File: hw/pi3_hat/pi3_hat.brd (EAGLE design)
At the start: 56.5 x 28.5 mm, 17 parts, among them U1 SINGLE-BIT_BUS_TRANSCEIVER, U2 SINGLE-BIT_BUS_TRANSCEIVER, U3 ST1S10, U4 DMMT5401, U5 DMG2305UX

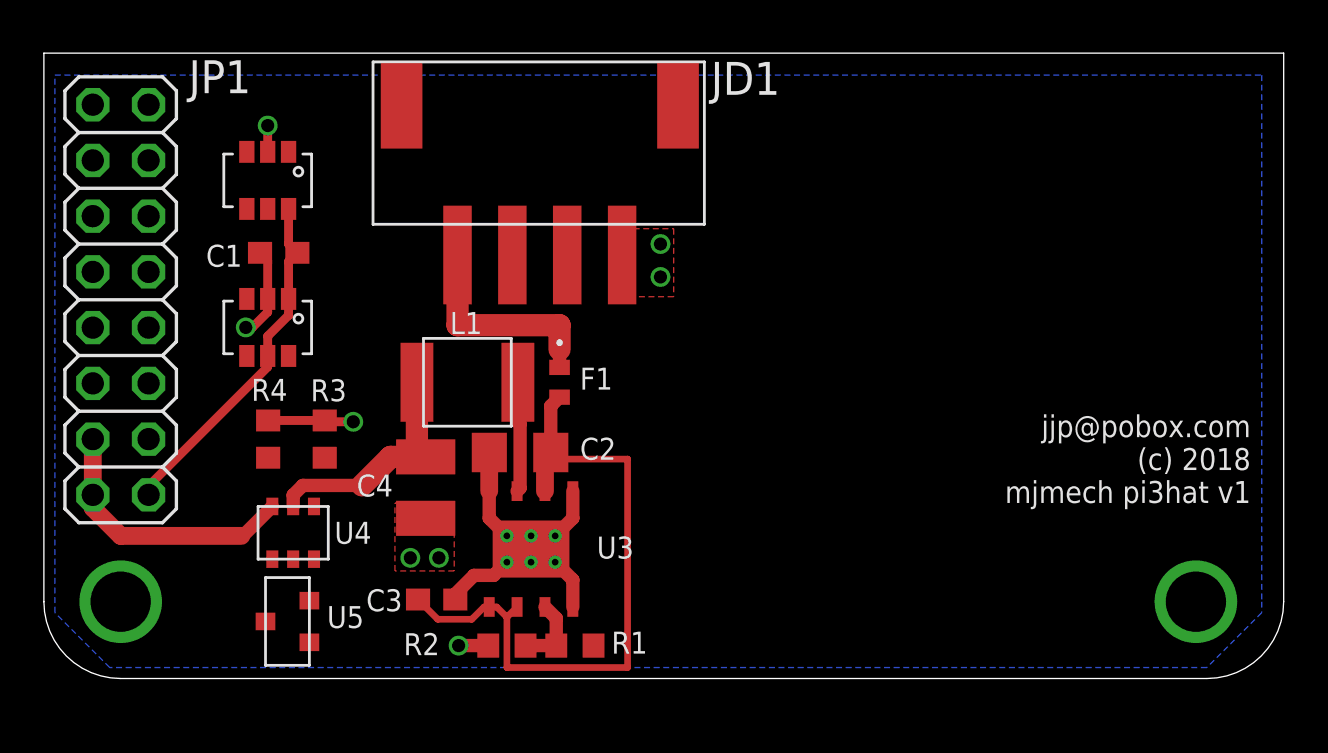
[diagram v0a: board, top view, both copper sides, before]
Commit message: rpi3 hat as sent to macrofab
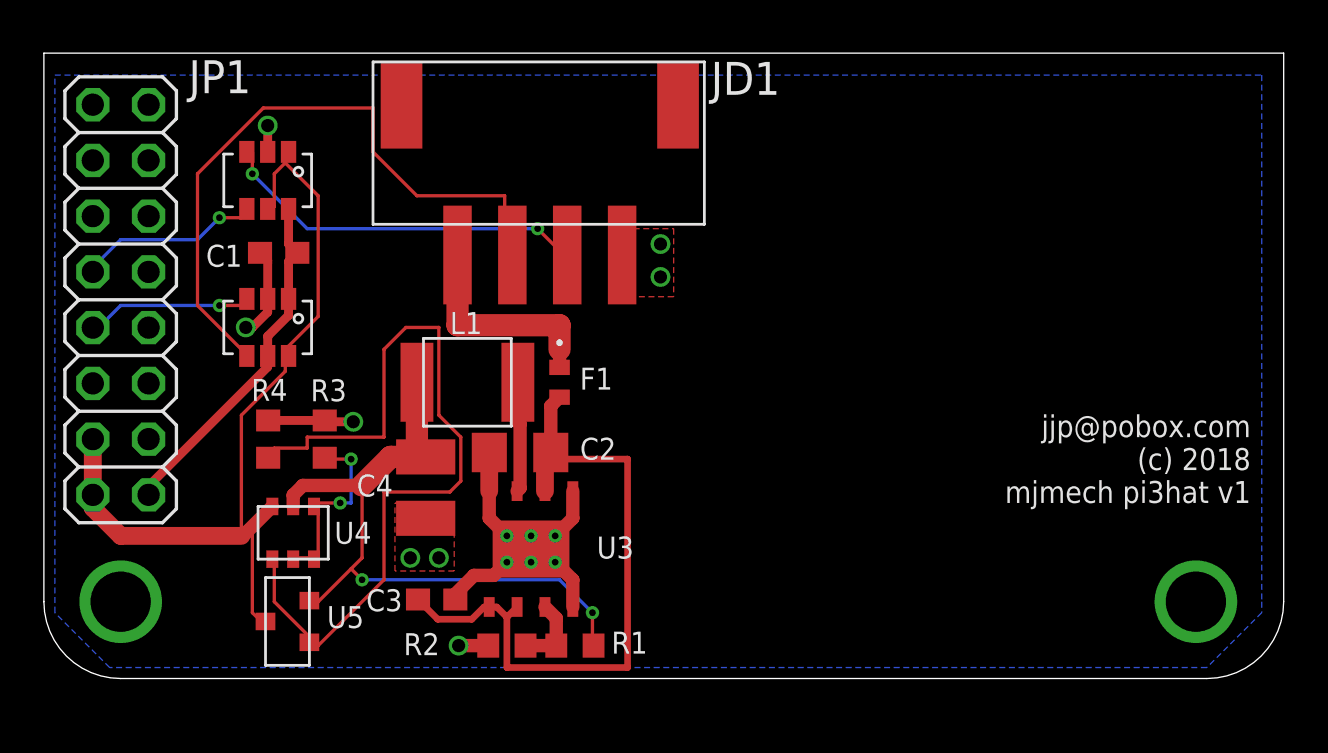
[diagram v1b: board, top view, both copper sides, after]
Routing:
- net N$5: track 0.00 -> 37.3 mm
- net PI_TX_5V: track 0.00 -> 30.2 mm
- net +5V: track 12.4 -> 39.4 mm
- net REGOUT: track 10.8 -> 30.8 mm, vias 0 -> 2
- net PI_RX_5V: track 0.00 -> 17.1 mm, vias 0 -> 2
- net N$1: track 0.00 -> 8.70 mm, vias 0 -> 2
- net N$2: track 0.00 -> 8.34 mm, vias 0 -> 1
- net N$4: track 0.00 -> 7.57 mm, vias 0 -> 1
- net GND: track 22.7 -> 23.4 mm

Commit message: Work on updated pi3 hat
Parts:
- added C10, C9: 10pF, mfpassives:C0603
- added C11, C12: .1uF, mfpassives:C0603
- added C13: 1uF, mfpassives:C0603
- added C5, C8: 22uF 16V, mfpassives:C1210
- added C6: 10uF 35V, mfpassives:C1206
- added C7: 1uF 16V, mfpassives:C0603
- added D1: MF-LED-0603-RED, mfleds:LED0603
- added D2: MF-LED-0603-GREEN, mfleds:LED0603
- added R5, R7, R8: 220, mfpassives:R0603
- added R6: 120, mfpassives:R0603
- added SWD: JST-ZH6SMT_VERT, controller:JST_B6B-ZR-SM4-TF(LF)(SN)
- added X1: 8.0MHz, controller:ABM3B
- C1: value 0.1uF -> .1uF; device rcl:C0603 -> mfpassives:C0603
- C2: value 10uF 16V -> 10uF 35V; device rcl:C1206 -> mfpassives:C1206
- C3: value 1uF 16V -> .1uF 50V; device rcl:C0603 -> mfpassives:C0805
- C4: value 22uF 16V -> 1uF; device rcl:C1210 -> mfpassives:C0603
- L1: value 3.3uH -> 6.8uH 3.7A; device odroid_shield:WURTH_74404042033 -> pi3_hat:TAIYO_8040
- R1: value 105k 1% -> 27k 1%; device rcl:R0603 -> mfpassives:R0603
- R2: value 20k 1% -> 5.1k 1%; device rcl:R0603 -> mfpassives:R0603
- U1: value SINGLE-BIT_BUS_TRANSCEIVER -> MAX13431E; device odroid_shield:SOT23-6 -> controller:TDFN10
- U2: value SINGLE-BIT_BUS_TRANSCEIVER -> RT829910L_DFN; device odroid_shield:SOT23-6 -> pi3_hat:10L_DFN
- U3: value ST1S10 -> STM32F051X6UFQFPN32; device odroid_shield:POWER_SO8 -> pi3_hat:UFQFPN32
- moved U2 40.1 mm to (50.0, 21.0), turned to 180 degrees
- moved C3 38.7 mm to (50.5, 24.5), turned to 90 degrees
- moved R2 35.6 mm to (52.6, 18.0), turned to 270 degrees
- moved R1 34.6 mm to (53.3, 20.3), turned to 180 degrees
- moved C2 28.3 mm to (45.9, 24.9), turned to 90 degrees
- moved L1 25.3 mm to (44.1, 18.5)
- moved F1 22.3 mm to (43.6, 23.2), turned to 0 degrees
- moved U1 15.8 mm to (22.8, 13.2), turned to 90 degrees
- moved C1 11.4 mm to (19.7, 12.4)
- moved U4 6.58 mm to (10.4, 13.1)
- moved U5 6.58 mm to (10.1, 9.10)
- moved C4 5.78 mm to (19.7, 14.0), turned to 180 degrees
- moved R3 5.70 mm to (11.3, 16.4)
- moved R4 3.20 mm to (7.72, 12.9)
- moved U3 1.30 mm to (21.5, 7.00), turned to 180 degrees
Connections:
- net N$7 renamed +18V
- removed net N$10: L1.1, U3.7
- removed net PI_RX_5V: JD1.2, U1.3
- removed net PI_TX_5V: JD1.3, U2.4
- removed net VCCIO: C1.1, JP1.1, U1.6, U2.1, U2.5
- new net +3V3: C1.P$1, C12.P$1, C13.P$1, C4.P$1, JP1.1, R7.P$2, R8.P$2, SWD.6, U1.1, U1.10, U3.1, U3.17, U3.5
- new net 485_DIR: U1.3, U1.4, U3.7
- new net 485_RX: U1.2, U3.9
- new net 485_TX: U1.5, U3.8
- new net N$12: SWD.5, U3.24
- new net N$15: D1.ANODE, R7.P$1
- new net N$16: D2.ANODE, R8.P$1
- new net N$17: D1.CATHODE, U3.26
- new net N$18: D2.CATHODE, U3.27
- new net N$35: C9.P$1, U3.3, X1.1
- new net N$36: C10.P$1, U3.2, X1.3
- new net N$8: C3.P$1, U2.5
- new net NRST: C11.P$1, SWD.2, U3.4
- new net PI_RX_3V: JP1.10, U3.19
- new net PI_TX_3V: JP1.8, U3.20
- new net POSTFUSE: C2.P$1, C6.P$1, F1.2, U2.6, U2.7
- new net RS485_N: JD1.3, R6.P$2, U1.9
- new net RS485_P: JD1.2, R6.P$1, U1.8
- new net SW: C3.P$2, L1.1, U2.8, U2.9
- net +5V: no longer U1.1, U1.5, U2.6
- net GND: now also C1.P$2, C10.P$2, C11.P$2, C12.P$2, C13.P$2, C2.P$2, C4.P$2, C5.P$2, C6.P$2, C7.P$2, C8.P$2, C9.P$2, R2.P$2, R5.P$2, SWD.4, U1.6, U1.PAD, U2.10, U2.P0, U2.P1, U2.P2, U3.P, X1.2, X1.4; no longer C1.2, C2.2, C3.2, C4.2, R2.1, U1.2, U2.2, U3.4, U3.5, U3.8, U3.PAD, U3.PAD1, U3.PAD2, U3.PAD3, U3.PAD4, U3.PAD5, U3.PAD6
- net N$11: now also R1.P$2, R2.P$1, U2.1; no longer C2.1, C3.1, F1.2, U3.1, U3.2, U3.6
- net N$13: now also SWD.3, U3.23; no longer R1.1, R2.2, U3.3
- net N$2: now also C7.P$1, U2.4; no longer JP1.10, U1.4
- net N$4: now also R5.P$1, U3.31; no longer JP1.8, U2.3
- net REGOUT: now also C5.P$1, C8.P$1, R1.P$1; no longer C4.1, R1.2
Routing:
- net N$5: track 37.3 -> 6.30 mm
- net PI_TX_5V: track 30.2 -> 0.00 mm
- net N$11: track 32.5 -> 2.82 mm
- net +5V: track 39.4 -> 19.7 mm, vias 0 -> 2
- net +3V3: track 0.00 -> 18.4 mm, vias 0 -> 6
- net PI_RX_5V: track 17.1 -> 0.00 mm, vias 2 -> 0
- net VCCIO: track 16.0 -> 0.00 mm
- net SW: track 0.00 -> 10.1 mm, vias 0 -> 2
- net +18V: track 9.77 -> 0.00 mm, vias 0 -> 6
- net N$36: track 0.00 -> 7.86 mm
- net N$4: track 7.57 -> 0.00 mm, vias 1 -> 0
- net N$2: track 8.34 -> 1.29 mm, vias 1 -> 0
- net RS485_P: track 0.00 -> 5.06 mm
- net N$10: track 5.06 -> 0.00 mm
- net RS485_N: track 0.00 -> 5.02 mm
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- added copper zone on layer 1, net +18V
- added copper zone on layer 15, net +18V
- added copper zone on layer 15, net +3V3
- added copper zone on layer 2, net GND
- added copper zone on layer 1, net POSTFUSE
- added copper zone on layer 1, net REGOUT
- added copper zone on layer 15, net REGOUT
- added copper zone on layer 1, net SW
- removed copper zone on layer 16, net GND
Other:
- board text added: "(c) 2019"
- board text added: "mjmech pi3hat r2"
- board text removed: "(c) 2018"
- board text removed: "mjmech pi3hat v1"

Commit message: Nominally complete pi3 hat
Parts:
- added R9: 220, mfpassives:R0603
- C1, C11, C12: value .1uF -> .1uF 50V; device mfpassives:C0603 -> mfpassives:C0805
- C7: value 1uF 16V -> 1uF
- R1: value 27k 1% -> 53.6k 1%
- R2: value 5.1k 1% -> 10k 1%
- R3: device rcl:R0603 -> mfpassives:R0603
- R4: value 47k 1% -> 53.6k 1%; device rcl:R0603 -> mfpassives:R0603
- R6: value 120 -> 220
- moved R6 7.10 mm to (22.6, 23.1), flipped to the bottom, turned to 0 degrees
- moved C12 0.42 mm to (25.5, 9.70)
- moved C1 0.40 mm to (19.3, 12.4)
- moved R4 0.29 mm to (7.70, 13.2), turned to 90 degrees
- moved C9 0.20 mm to (28.1, 8.70)
- moved C4 0.20 mm to (19.7, 14.2)
- turned R3 to 90 degrees
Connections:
- net GND: now also R3.P$2, R4.P$2; no longer R3.1, R4.1
- net N$1: now also R3.P$1; no longer R3.2
- net N$5: now also R4.P$1; no longer R4.2
- net RS485_N: now also JD1.2, R6.P$1, R9.P$1; no longer JD1.3, R6.P$2
- net RS485_P: now also JD1.3, R6.P$2, R9.P$2; no longer JD1.2, R6.P$1
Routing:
- net N$13: track 0.00 -> 42.6 mm
- net PI_TX_3V: track 0.00 -> 30.5 mm
- net PI_RX_3V: track 0.00 -> 27.4 mm
- net N$12: track 0.00 -> 21.3 mm, vias 0 -> 2
- net NRST: track 4.91 -> 23.2 mm
- net RS485_N: track 5.02 -> 11.5 mm, vias 0 -> 3
- net RS485_P: track 5.06 -> 11.3 mm, vias 0 -> 1
- net 485_DIR: track 0.00 -> 5.22 mm, vias 0 -> 2
- net 485_TX: track 0.00 -> 3.00 mm
- net 485_RX: track 0.00 -> 2.76 mm
- net N$4: track 0.00 -> 1.73 mm
- net +3V3: track 18.4 -> 19.7 mm
